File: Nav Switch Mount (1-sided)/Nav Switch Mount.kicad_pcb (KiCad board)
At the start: 2 copper layers, 22.3 x 12.6 mm, 9 parts, among them J1 Conn_01x06, U1 SKQUAAA010

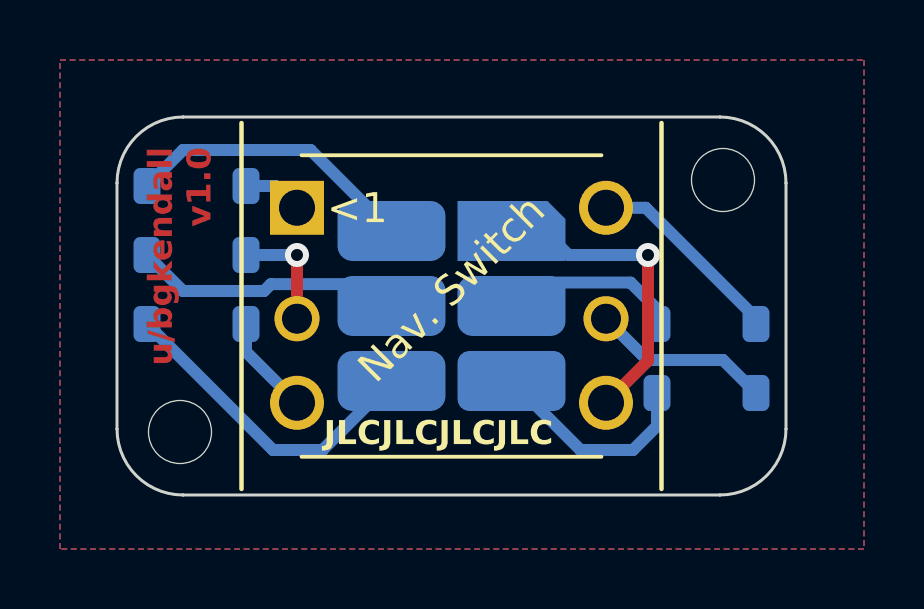
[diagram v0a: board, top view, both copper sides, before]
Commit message: First version of 1-sided variant
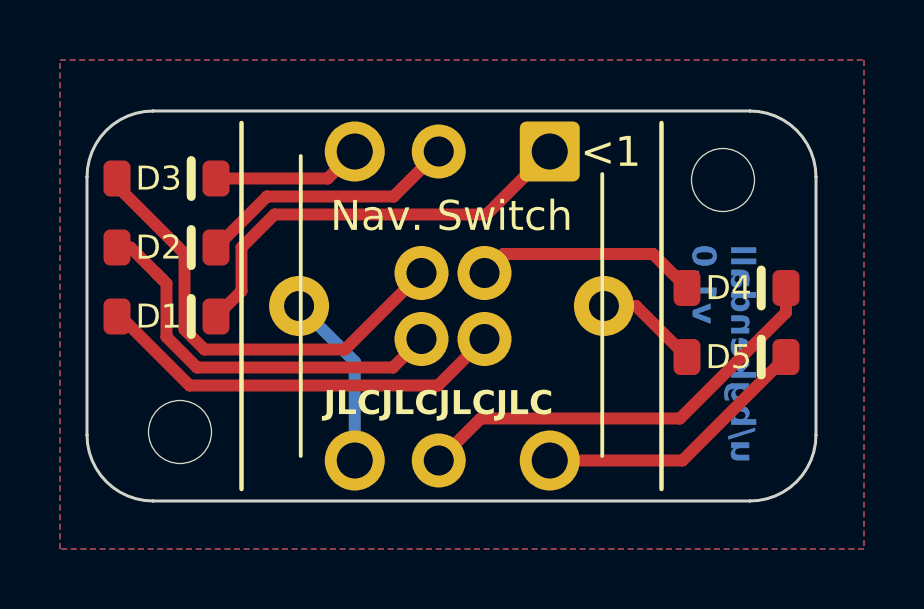
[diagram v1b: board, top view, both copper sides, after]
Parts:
- D1, D2, D3, D4, D5: moved to F.Cu
- moved D3 4.95 mm to (149.6, 47.8)
- moved D1 4.46 mm to (149.6, 52.4)
- moved D4 3.64 mm to (168.6, 51.4)
- moved D5 1.49 mm to (168.6, 53.7)
- moved D2 1.03 mm to (149.6, 50.0)
- turned U1 to -90 degrees
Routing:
- net Net-(D1-K): track 2.00 -> 14.3 mm
- net Net-(D4-K): track 6.03 -> 14.4 mm
- net Net-(D2-A): track 8.01 -> 13.6 mm
- net Net-(D2-K): track 3.83 -> 8.75 mm, vias 1 -> 0
- net Net-(D3-A): track 10.8 -> 14.9 mm
- net Net-(D1-A): track 9.77 -> 13.8 mm
- net Net-(D5-K): track 6.52 -> 9.30 mm
- net Net-(J1-Pin_6): track 8.93 -> 6.78 mm, vias 1 -> 0
- net Net-(D3-K): track 3.33 -> 5.00 mm
- net Net-(D5-A): track 4.94 -> 3.47 mm
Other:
- board size 22.3 x 12.6 mm -> 24.3 x 13 mm
- board text removed: "<1"
